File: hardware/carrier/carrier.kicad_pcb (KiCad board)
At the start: 4 copper layers, 165 x 103 mm, 157 parts, among them J1 Harness_4Runner, J2 Pi 4 GPIO, J3 UART, M1 FAN1, M2 FAN2, Q1 BUK7Y4R8-60E, Q2 BUK7Y4R8-60E, Q3 MMBT3904, Q4 MMBT3904, Q5 MMBT3904, Q6 2N7002, Q7 2N7002, U1 LM74800-Q1, U2 ADS1115IDGS, U3 DS3231SN, U4 CAT24C32, U5 LM61460-Q1, U6 TLV75533PDBV, U7 TAS6424E-Q1, U8 PCM1808-Q1, X1 12.288MHz

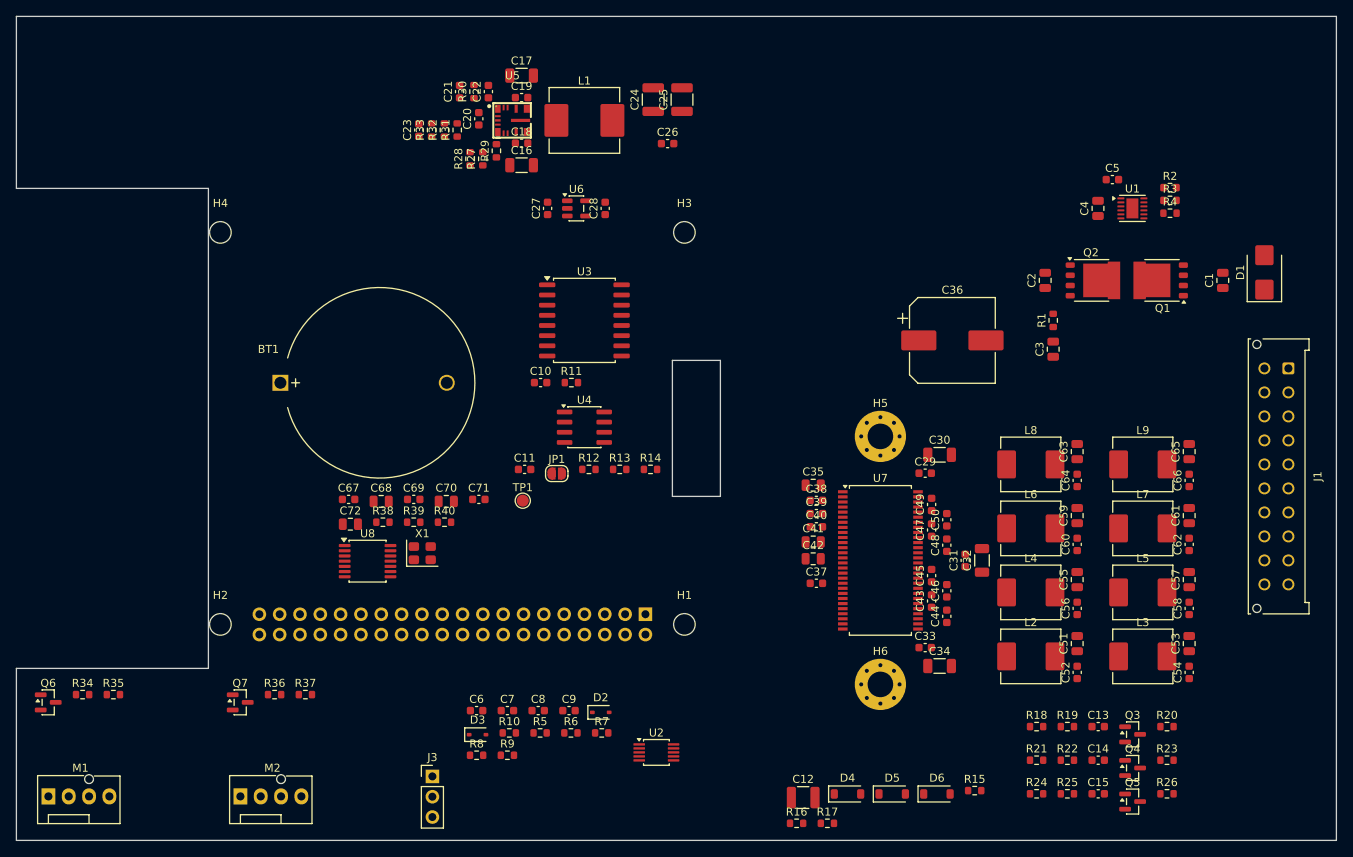
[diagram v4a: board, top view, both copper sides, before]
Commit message: Carrier: measured Pi position, re-floorplan, 3D stack-up
The Pi's spot on the Hosyond display, measured from the maker's back-view
drawing scaled by the Pi's own 58 x 49 mm hole pattern: holes at x 58.8 /
116.8, y 35.1 / 84.1 from the display's top-left corner (back view), Pi
turned 180 degrees with the ports toward the screen's right. The pogo
pads line up with GPIO 2/4/6, which confirms it.

The Pi sits mid-screen, so the board gets a notch from the port block to
the left edge (tall Ethernet jack, cable access). New floorplan: harness
plug on the top edge, protection and RTC along the top, amp turned 90
degrees with its heatsink along the right edge, buck over the Pi next to
its 5 V pins, clocks and fans at the bottom. DRC: no overlaps.

tools/assembly.py builds the display + Pi 4 + board + heatsink stack as
STEP/STL (165 x 103 x 56.5 mm); tools/render3d.py draws review views.

Co-Authored-By: Claude Opus 5.5 <noreply@anthropic.com>
Claude-Session: https://claude.ai/code/session_01EoLoLi7g91W5u4w3UzwQgu
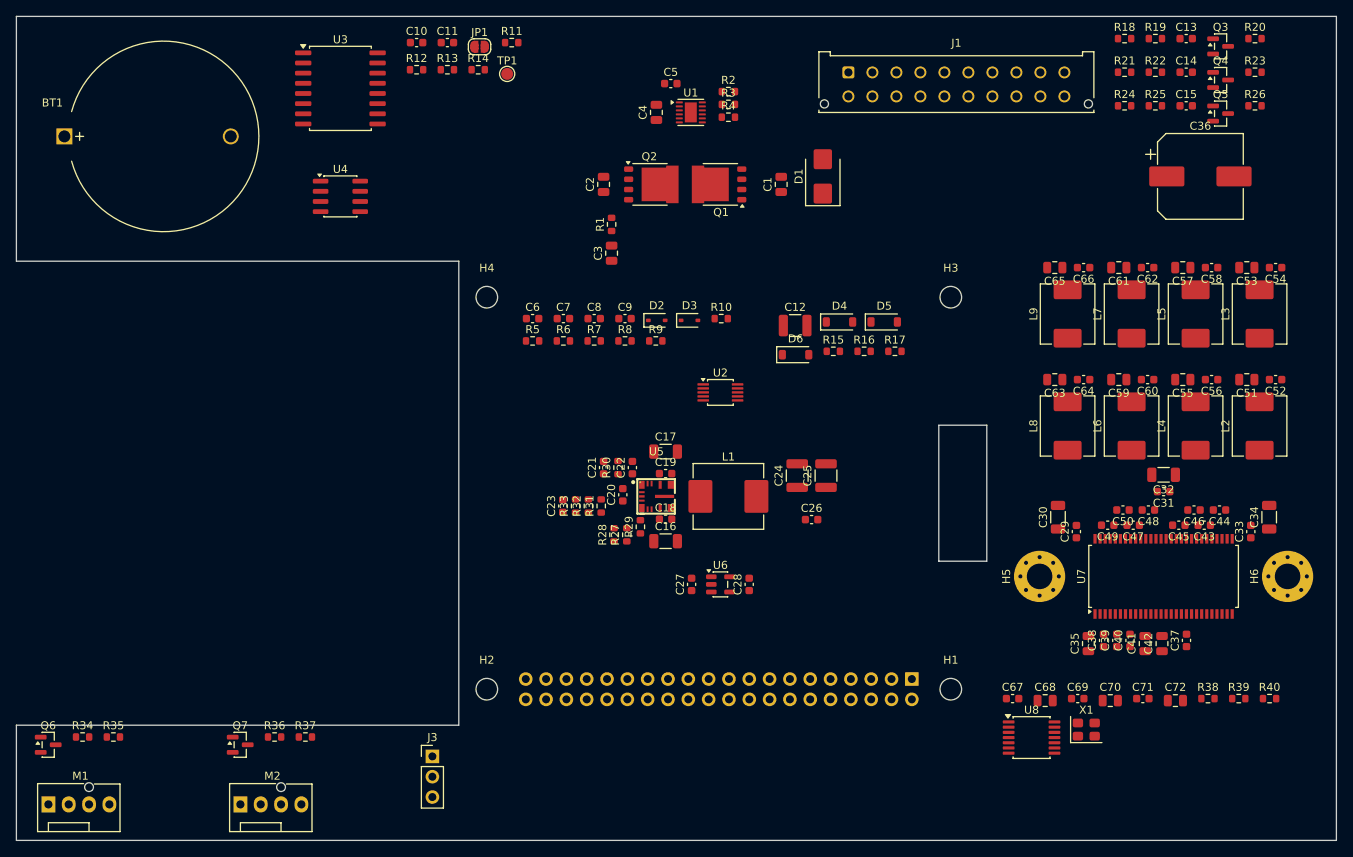
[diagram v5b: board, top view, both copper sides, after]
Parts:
- moved C72 105.5 mm to (244.9, 185.5)
- moved R38 105.5 mm to (248.9, 185.3)
- moved R39 105.5 mm to (252.8, 185.3)
- moved R40 105.5 mm to (256.6, 185.3)
- moved C13 86.7 mm to (246.2, 102.8)
- moved C14 86.7 mm to (246.2, 107.0)
- moved Q3 86.7 mm to (250.5, 103.7)
- moved Q4 86.7 mm to (250.5, 107.9)
- moved R18 86.7 mm to (238.5, 102.8)
- moved R19 86.7 mm to (242.4, 102.8)
- moved R20 86.7 mm to (254.8, 102.8)
- moved R21 86.7 mm to (238.5, 107.0)
- moved R22 86.7 mm to (242.4, 107.0)
- moved R23 86.7 mm to (254.8, 107.0)
- moved C15 86.7 mm to (246.2, 111.2)
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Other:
- outline, holes or cut-outs redrawn

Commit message: Carrier: route the board
Four layers: In1 solid GND, In2 split between +12V_PROT and +5V. Power
paths are pours and hand-placed tracks (battery path, buck loop, amp
PVDD, the Pi's 5 V pins); the amp outputs and speaker tracks are routed
by script, P legs on top and M legs under the coils, speaker lanes
nested so none cross. Every GND pad has its own via to the plane. The
rest goes through Freerouting, with a small grid router for the tight
spots. Nothing copper within 3 mm of the outer edge, so a small error in
the Pi position only moves the outline. DRC: 0 errors, 0 unrouted.

Changes made along the way:
- amp channels remapped (ch1..4 = RL, RR, FL, FR) and the harness
  speaker pins reordered (3/13 FR, 4/14 FL, 5/15 RR, 6/16 RL) so the
  speaker tracks run straight; tas6424.py follows
- P-leg boot caps turned and all eight centred on their pin pairs
- coils moved up to open room for the output escapes; centre PVDD caps
  and the 470 uF bulk moved
- LM74800 turned 180 degrees so each pin row faces its parts; C4, C5
  and the OV divider rearranged to match
- fan tach pull-ups moved beside the Pi header
- net classes were being dropped when the board was saved; fixed

tools/build_board.sh rebuilds everything. tools/fit_plate.py makes a
printable plate to check the fit on the screen before ordering.

Co-Authored-By: Claude Opus 5.5 <noreply@anthropic.com>
Claude-Session: https://claude.ai/code/session_01EoLoLi7g91W5u4w3UzwQgu
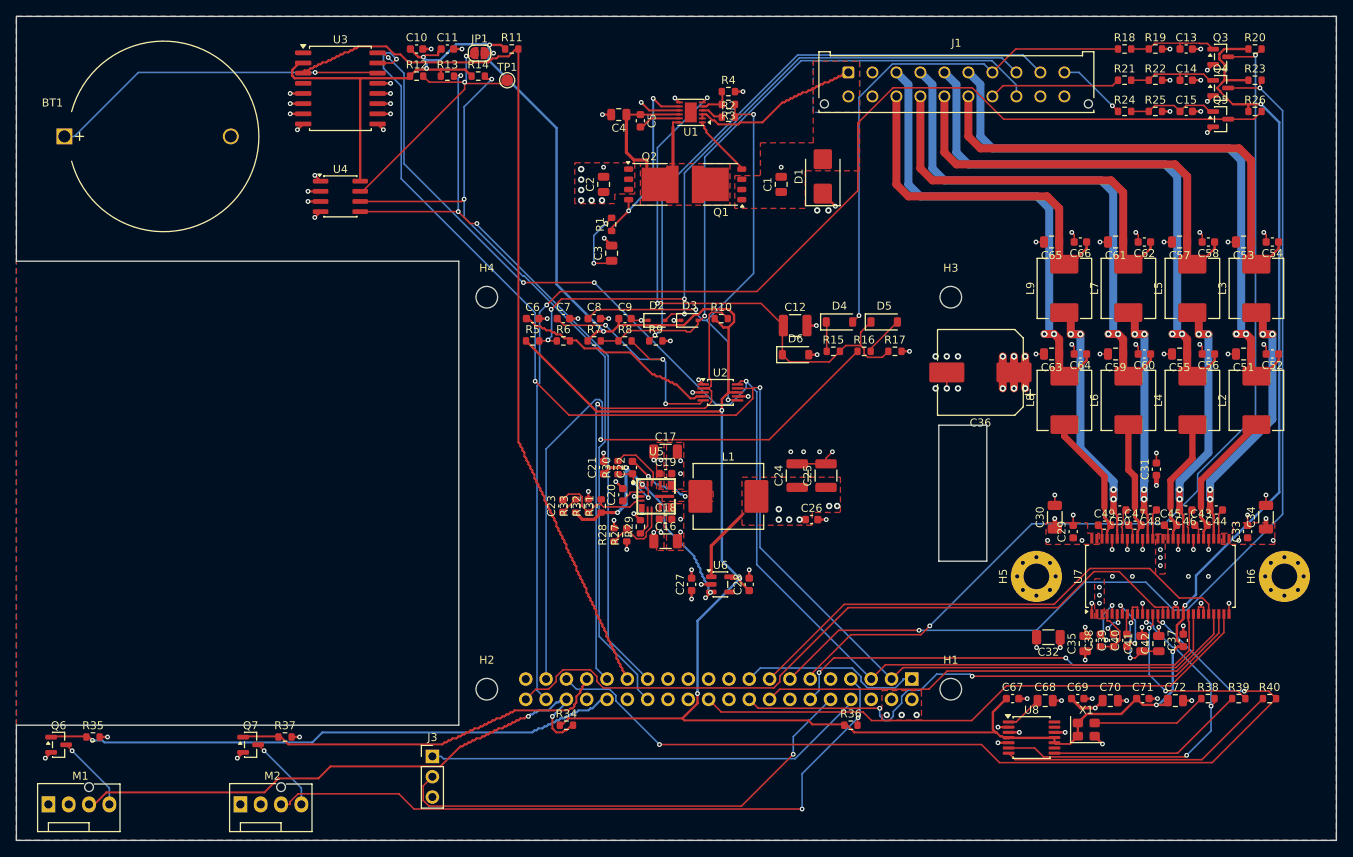
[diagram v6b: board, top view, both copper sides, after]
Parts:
- moved R36 72.1 mm to (204.3, 188.6)
- moved R34 60.5 mm to (168.8, 188.6)
- moved C36 36.8 mm to (220.5, 144.5), turned to 180 degrees
- moved C32 24.9 mm to (229.0, 177.6)
- moved C5 6.01 mm to (178.0, 113.0), turned to -90 degrees
- moved C4 4.71 mm to (175.3, 112.3), turned to 180 degrees
- moved C51 3.22 mm to (253.4, 142.2)
- moved C53 3.22 mm to (253.4, 128.2)
- moved C55 3.22 mm to (245.4, 142.2)
- moved C56 3.22 mm to (249.0, 142.2)
- moved C57 3.22 mm to (245.4, 128.2)
- moved C58 3.22 mm to (249.0, 128.2)
- moved C59 3.22 mm to (237.4, 142.2)
- moved C60 3.22 mm to (241.0, 142.2)
- moved C61 3.22 mm to (237.4, 128.2)
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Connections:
- C43 pad 2: /AMP_FL+ -> /AMP_RL+
- C44 pad 2: /AMP_FL- -> /AMP_RL-
- C45 pad 2: /AMP_FR+ -> /AMP_RR+
- C46 pad 2: /AMP_FR- -> /AMP_RR-
- C47 pad 2: /AMP_RL+ -> /AMP_FL+
- C48 pad 2: /AMP_RL- -> /AMP_FL-
- C49 pad 2: /AMP_RR+ -> /AMP_FR+
- C50 pad 2: /AMP_RR- -> /AMP_FR-
- C51 pad 1: /SPK_FL+ -> /SPK_RL+
- C52 pad 1: /SPK_FL+ -> /SPK_RL+
- C53 pad 1: /SPK_FL- -> /SPK_RL-
- C54 pad 1: /SPK_FL- -> /SPK_RL-
- C55 pad 1: /SPK_FR+ -> /SPK_RR+
- C56 pad 1: /SPK_FR+ -> /SPK_RR+
- C57 pad 1: /SPK_FR- -> /SPK_RR-
- C58 pad 1: /SPK_FR- -> /SPK_RR-
- C59 pad 1: /SPK_RL+ -> /SPK_FL+
- C60 pad 1: /SPK_RL+ -> /SPK_FL+
- C61 pad 1: /SPK_RL- -> /SPK_FL-
- C62 pad 1: /SPK_RL- -> /SPK_FL-
- C63 pad 1: /SPK_RR+ -> /SPK_FR+
- C64 pad 1: /SPK_RR+ -> /SPK_FR+
- C65 pad 1: /SPK_RR- -> /SPK_FR-
- C66 pad 1: /SPK_RR- -> /SPK_FR-
- J1 pad 13: /SPK_FL- -> /SPK_FR-
- J1 pad 14: /SPK_FR- -> /SPK_FL-
- J1 pad 15: /SPK_RL- -> /SPK_RR-
- J1 pad 16: /SPK_RR- -> /SPK_RL-
- J1 pad 3: /SPK_FL+ -> /SPK_FR+
- J1 pad 4: /SPK_FR+ -> /SPK_FL+
- J1 pad 5: /SPK_RL+ -> /SPK_RR+
- J1 pad 6: /SPK_RR+ -> /SPK_RL+
- L2 pad 1: /AMP_FL+ -> /AMP_RL+
- L2 pad 2: /SPK_FL+ -> /SPK_RL+
- L3 pad 1: /AMP_FL- -> /AMP_RL-
- L3 pad 2: /SPK_FL- -> /SPK_RL-
- L4 pad 1: /AMP_FR+ -> /AMP_RR+
- L4 pad 2: /SPK_FR+ -> /SPK_RR+
- L5 pad 1: /AMP_FR- -> /AMP_RR-
- L5 pad 2: /SPK_FR- -> /SPK_RR-
- L6 pad 1: /AMP_RL+ -> /AMP_FL+
- L6 pad 2: /SPK_RL+ -> /SPK_FL+
- L7 pad 1: /AMP_RL- -> /AMP_FL-
- L7 pad 2: /SPK_RL- -> /SPK_FL-
- L8 pad 1: /AMP_RR+ -> /AMP_FR+
- L8 pad 2: /SPK_RR+ -> /SPK_FR+
- L9 pad 1: /AMP_RR- -> /AMP_FR-
- L9 pad 2: /SPK_RR- -> /SPK_FR-
- U7 pad 32: /AMP_FL- -> /AMP_RL-
- U7 pad 34: /AMP_FL+ -> /AMP_RL+
- U7 pad 38: /AMP_FR- -> /AMP_RR-
- U7 pad 40: /AMP_FR+ -> /AMP_RR+
- U7 pad 45: /AMP_RL- -> /AMP_FL-
- U7 pad 47: /AMP_RL+ -> /AMP_FL+
- U7 pad 51: /AMP_RR- -> /AMP_FR-
- U7 pad 53: /AMP_RR+ -> /AMP_FR+
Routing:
- net +3V3: track 0.00 -> 400.2 mm, vias 0 -> 11
- net /I2C_SDA: track 0.00 -> 174.2 mm, vias 0 -> 3
- net /I2C_SCL: track 0.00 -> 163.4 mm, vias 0 -> 4
- net /~{REVERSE}: track 0.00 -> 157.8 mm, vias 0 -> 1
- net GND: track 0.00 -> 134.1 mm, vias 0 -> 125
- net /~{LIGHTS_ON}: track 0.00 -> 132.5 mm, vias 0 -> 2
- net /~{ACC_ON}: track 0.00 -> 120.5 mm, vias 0 -> 2
- net /I2S_FSYNC: track 0.00 -> 116.4 mm, vias 0 -> 3
- net /~{RTC_INT}: track 0.00 -> 114.7 mm
- net /ID_SCL: track 0.00 -> 103.3 mm, vias 0 -> 2
- net /ID_SDA: track 0.00 -> 99.0 mm, vias 0 -> 3
- net /I2S_DOUT: track 0.00 -> 93.5 mm
- net /SWC1_IN: track 0.00 -> 92.1 mm, vias 0 -> 4
- net /FAN2_TACH: track 0.00 -> 87.3 mm, vias 0 -> 2
- net /SWC2_IN: track 0.00 -> 81.2 mm, vias 0 -> 1
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- added copper zone on F.Cu, net +12V_PROT
- added copper zone on In2.Cu, net +12V_PROT
- added copper zone on F.Cu, net +5V
- added copper zone on In2.Cu, net +5V
- added copper zone on B.Cu, net /+12V_BATT
- added copper zone on F.Cu, net /+12V_BATT
- added copper zone on F.Cu, net /SW_5V
- added copper zone on F.Cu, net /VMID
- added copper zone on B.Cu, net GND
- added copper zone on F.Cu, net GND
- added copper zone on In1.Cu, net GND
- added copper zone on In2.Cu, net GND

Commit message: Carrier: 3D models for the harness plug and coin holder, credit text
KiCad ships no model for the Micro-Fit 43045 or the MYOUNG CR2032
holder: STEP models from LCSC/EasyEDA in lib/3d, placed on KiCad's
footprint origins. Top silkscreen credit in the bottom strip.

Co-Authored-By: Claude Opus 5.5 <noreply@anthropic.com>
Claude-Session: https://claude.ai/code/session_01EoLoLi7g91W5u4w3UzwQgu
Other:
- board text added: "@ajxd2 Anthony Kovach"
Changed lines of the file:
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@@
 		)
 		(embedded_fonts no)
-		(model "${KICAD10_3DMODEL_DIR}/Connector_Molex.3dshapes/Molex_Micro-Fit_3.0_43045-2012_2x10_P3.00mm_Vertical.step"
+		(model "${KIPRJMOD}/lib/3d/easyeda.3dshapes/CONN-TH_20P-P3.00_430452012.step"
 			(offset
-				(xyz 0 0 0)
+				(xyz 13.5 -1.505 0)
 			)
 			(scale
@@
 			)
 			(rotate
-				(xyz 0 0 0)
+				(xyz 0 0 180)
 			)
 		)
@@
 		)
 		(embedded_fonts no)
-		(model "${KICAD10_3DMODEL_DIR}/Battery.3dshapes/BatteryHolder_MYOUNG_BS-07-A1BJ001_CR2032.step"
+		(model "${KIPRJMOD}/lib/3d/easyeda.3dshapes/BAT-TH_BS-07-A1BJ001.step"
 			(offset
-				(xyz 0 0 0)
+				(xyz 14.23 0 0)
 			)
 			(scale
@@
 		(layer "F.Fab")
 	)
+	(gr_text "@ajxd2  Anthony Kovach"
+		(at 190 196.3 0)
+		(layer "F.SilkS")
+		(effects
+			(font
+				(size 2 2)
+				(thickness 0.3)
+			)
+		)
+	)
 	(gr_text "HEATSINK 20x41.4 (mech/heatsink.step): parts under it < 2.2 mm"

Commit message: Carrier: board name and revision, message on the underside
Top: 4RUNNER CARPLAY CARRIER REV A up the strip beside the Pi. Underside,
facing the Pi: NO FIDDLING WHILE DRIVING, the board's spec and date.

Co-Authored-By: Claude Opus 5.5 <noreply@anthropic.com>
Claude-Session: https://claude.ai/code/session_01EoLoLi7g91W5u4w3UzwQgu
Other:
- board text added: "2007 4RUNNER / PI 4 / 4 x 25 W CLASS D"
- board text added: "4RUNNER CARPLAY CARRIER REV A"
- board text added: "NO FIDDLING WHILE DRIVING"
- board text added: "REV A 2026-09"
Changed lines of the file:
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@@
 		(layer "F.Fab")
+	)
+	(gr_text "4RUNNER CARPLAY CARRIER  REV A"
+		(at 158.3 159.6 90)
+		(layer "F.SilkS")
+		(effects
+			(font
+				(size 1.4 1.4)
+				(thickness 0.22)
+			)
+		)
 	)
 	(gr_text "@ajxd2  Anthony Kovach"
@@
 		)
 	)
+	(gr_text "2007 4RUNNER  /  PI 4  /  4 x 25 W CLASS D"
+		(at 188 155 0)
+		(layer "B.SilkS")
+		(effects
+			(font
+				(size 1.3 1.3)
+				(thickness 0.22)
+			)
+			(justify mirror)
+		)
+	)
+	(gr_text "REV A  2026-09"
+		(at 188 158.5 0)
+		(layer "B.SilkS")
+		(effects
+			(font
+				(size 1.3 1.3)
+				(thickness 0.22)
+			)
+			(justify mirror)
+		)
+	)
+	(gr_text "NO FIDDLING WHILE DRIVING"
+		(at 188 150 0)
+		(layer "B.SilkS")
+		(effects
+			(font
+				(size 2.2 2.2)
+				(thickness 0.3)
+			)
+			(justify mirror)
+		)
+	)
